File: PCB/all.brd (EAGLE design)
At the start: 49.8 x 49.8 mm, 41 parts, among them J1 ISP Programmer, U1 ATMEGA32U4, U2 3.3V_REG, U3 MPU-6050-1, U5 MCP73831, U6 AL8805, X1 USBSMD

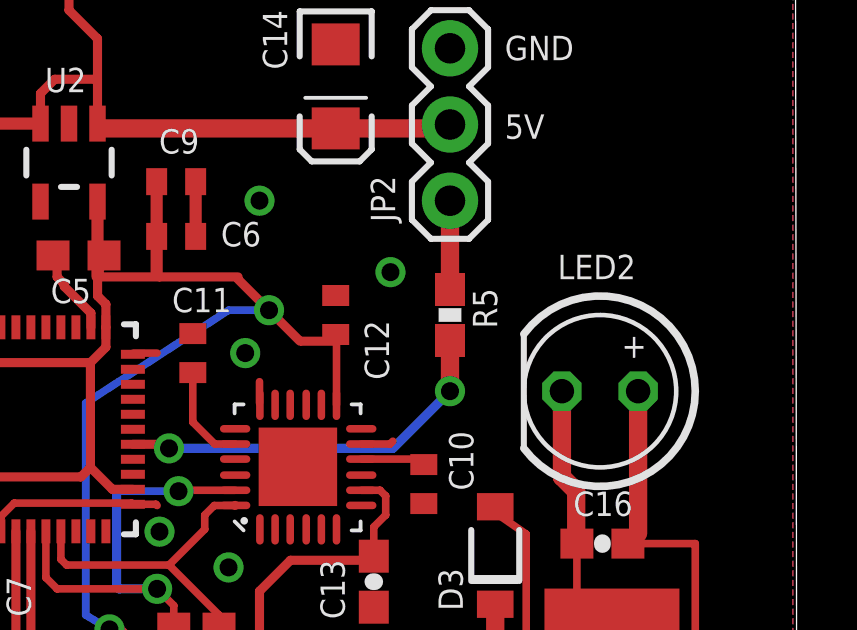
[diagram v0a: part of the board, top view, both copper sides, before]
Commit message: added 3D models
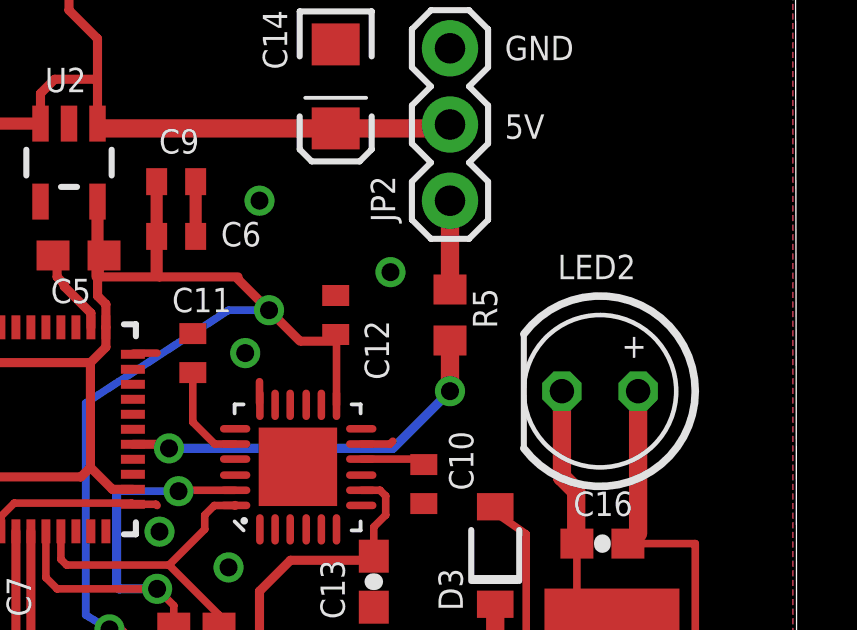
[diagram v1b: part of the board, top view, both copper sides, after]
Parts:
- R5: device SparkFun:0603-RES -> rcl:R0603
- U1: device SparkFun:QFN-44-NOPAD -> SparkFun-Retired:SPARKFUN-DIGITALIC_QFN-44-NOPAD
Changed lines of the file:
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@@
 <?xml version="1.0" encoding="utf-8"?>
 <!DOCTYPE eagle SYSTEM "eagle.dtd">
-<eagle version="7.4.0">
+<eagle version="7.3.0">
 <drawing>
 <settings>
@@
 <layers>
 <layer number="1" name="Top" color="4" fill="1" visible="yes" active="yes"/>
+<layer number="2" name="Route2" color="1" fill="3" visible="no" active="yes"/>
+<layer number="3" name="Route3" color="4" fill="3" visible="no" active="yes"/>
+<layer number="4" name="Route4" color="1" fill="4" visible="no" active="yes"/>
+<layer number="5" name="Route5" color="4" fill="4" visible="no" active="yes"/>
+<layer number="6" name="Route6" color="1" fill="8" visible="no" active="yes"/>
+<layer number="7" name="Route7" color="4" fill="8" visible="no" active="yes"/>
+<layer number="8" name="Route8" color="1" fill="2" visible="no" active="yes"/>
+<layer number="9" name="Route9" color="4" fill="2" visible="no" active="yes"/>
+<layer number="10" name="Route10" color="1" fill="7" visible="no" active="yes"/>
+<layer number="11" name="Route11" color="4" fill="7" visible="no" active="yes"/>
+<layer number="12" name="Route12" color="1" fill="5" visible="no" active="yes"/>
+<layer number="13" name="Route13" color="4" fill="5" visible="no" active="yes"/>
+<layer number="14" name="Route14" color="1" fill="6" visible="no" active="yes"/>
+<layer number="15" name="Route15" color="4" fill="6" visible="no" active="yes"/>
 <layer number="16" name="Bottom" color="1" fill="1" visible="yes" active="yes"/>
 <layer number="17" name="Pads" color="2" fill="1" visible="yes" active="yes"/>
@@
 <layer number="54" name="bGND_GNDA" color="1" fill="9" visible="no" active="no"/>
 <layer number="56" name="wert" color="7" fill="1" visible="no" active="no"/>
+<layer number="57" name="tCAD" color="7" fill="1" visible="no" active="no"/>
+<layer number="59" name="tCarbon" color="7" fill="1" visible="no" active="no"/>
+<layer number="60" name="bCarbon" color="7" fill="1" visible="no" active="no"/>
+<layer number="90" name="Modules" color="5" fill="1" visible="no" active="no"/>
 <layer number="91" name="Nets" color="2" fill="1" visible="no" active="no"/>
 <layer number="92" name="Busses" color="1" fill="1" visible="no" active="no"/>
@@
 <layer number="108" name="tplace-old" color="10" fill="1" visible="no" active="yes"/>
 <layer number="109" name="ref-old" color="11" fill="1" visible="no" active="yes"/>
+<layer number="110" name="fp0" color="7" fill="1" visible="no" active="yes"/>
+<layer number="111" name="LPC17xx" color="7" fill="1" visible="no" active="yes"/>
+<layer number="112" name="tSilk" color="7" fill="1" visible="no" active="yes"/>
+<layer number="113" name="IDFDebug" color="4" fill="1" visible="no" active="yes"/>
 <layer number="116" name="Patch_BOT" color="9" fill="4" visible="no" active="yes"/>
 <layer number="121" name="_tsilk" color="7" fill="1" visible="no" active="yes"/>
 <layer number="122" name="_bsilk" color="7" fill="1" visible="no" active="yes"/>
+<layer number="123" name="tTestmark" color="7" fill="1" visible="no" active="yes"/>
+<layer number="124" name="bTestmark" color="7" fill="1" visible="no" active="yes"/>
 <layer number="125" name="_tNames" color="7" fill="1" visible="no" active="yes"/>
+<layer number="126" name="_bNames" color="7" fill="1" visible="no" active="yes"/>
+<layer number="127" name="_tValues" color="7" fill="1" visible="no" active="yes"/>
+<layer number="128" name="_bValues" color="7" fill="1" visible="no" active="yes"/>
+<layer number="129" name="Mask" color="7" fill="1" visible="yes" active="yes"/>
+<layer number="131" name="tAdjust" color="7" fill="1" visible="no" active="yes"/>
+<layer number="132" name="bAdjust" color="7" fill="1" visible="no" active="yes"/>
 <layer number="144" name="Drill_legend" color="7" fill="1" visible="no" active="yes"/>
+<layer number="150" name="Notes" color="7" fill="1" visible="no" active="yes"/>
 <layer number="151" name="HeatSink" color="7" fill="1" visible="no" active="yes"/>
+<layer number="152" name="_bDocu" color="7" fill="1" visible="no" active="yes"/>
+<layer number="153" name="FabDoc1" color="7" fill="1" visible="no" active="yes"/>
+<layer number="154" name="FabDoc2" color="7" fill="1" visible="no" active="yes"/>
+<layer number="155" name="FabDoc3" color="7" fill="1" visible="no" active="yes"/>
 <layer number="199" name="Contour" color="7" fill="1" visible="no" active="yes"/>
 <layer number="200" name="200bmp" color="1" fill="10" visible="no" active="yes"/>
@@
 <layer number="220" name="220bmp" color="21" fill="1" visible="no" active="no"/>
 <layer number="221" name="221bmp" color="22" fill="1" visible="no" active="no"/>
-<layer number="222" name="222bmp" color="23" fill="1" visible="no" active="no"/>
 <layer number="223" name="223bmp" color="24" fill="1" visible="no" active="no"/>
 <layer number="224" name="224bmp" color="25" fill="1" visible="no" active="no"/>
+<layer number="225" name="225bmp" color="7" fill="1" visible="yes" active="yes"/>
+<layer number="226" name="226bmp" color="7" fill="1" visible="yes" active="yes"/>
+<layer number="227" name="227bmp" color="7" fill="1" visible="yes" active="yes"/>
+<layer number="228" name="228bmp" color="7" fill="1" visible="yes" active="yes"/>
+<layer number="229" name="229bmp" color="7" fill="1" visible="yes" active="yes"/>
+<layer number="230" name="230bmp" color="7" fill="1" visible="yes" active="yes"/>
+<layer number="231" name="231bmp" color="7" fill="1" visible="yes" active="yes"/>
+<layer number="248" name="Housing" color="7" fill="1" visible="no" active="yes"/>
+<layer number="249" name="Edge" color="7" fill="1" visible="no" active="yes"/>
 <layer number="250" name="Descript" color="3" fill="1" visible="no" active="no"/>
 <layer number="251" name="SMDround" color="12" fill="11" visible="no" active="no"/>
 <layer number="254" name="cooling" color="7" fill="1" visible="no" active="yes"/>
+<layer number="255" name="routoute" color="7" fill="1" visible="yes" active="yes"/>
 </layers>
 <board>
@@
 </autorouter>
 <elements>
-<element name="U1" library="SparkFun" package="QFN-44-NOPAD" value="ATMEGA32U4" x="24.13" y="21.59" smashed="yes">
+<element name="U1" library="SparkFun-Retired" package="SPARKFUN-DIGITALIC_QFN-44-NOPAD" value="ATMEGA32U4" x="24.13" y="21.59" smashed="yes">
 <attribute name="NAME" x="19.29875" y="24.881875" size="0.8128" layer="25"/>
 <attribute name="VALUE" x="21.63" y="15.44" size="1.27" layer="27"/>
@@
 <attribute name="VALUE" x="41.275" y="27.94" size="1.27" layer="27" rot="R90"/>
 </element>
-<element name="R5" library="SparkFun" package="0603-RES" value="300" x="38.1" y="25.4" smashed="yes" rot="R270">
+<element name="R5" library="rcl" package="R0603" value="300" x="38.1" y="25.4" smashed="yes" rot="R270">
 <attribute name="NAME" x="38.862" y="26.289" size="0.8128" layer="25" font="vector" rot="R270"/>
 <attribute name="VALUE" x="36.957" y="26.416" size="0.4064" layer="27" font="vector" rot="R270"/>

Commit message: Adding Qi receiver modules
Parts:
- removed F1: PTCSMD, SparkFun:PTC-1206
- removed XTAL1: 16MHz, SparkFun:CRYSTAL-SMD-5X3
- added C18, C19, C20, C21, C22, C23, C24, C25, C26, C27, C28, C29: 10μF, SparkFun:EIA3216
- added CP1, CP2, CP3, CP4, CP5, CP6, CP7, CP8, CS, CS10, CS17, CS20, CS27, CS30, CS37, CS7: 18pF, rcl:C0603
- added CS1, CS11, CS12, CS2, CS21, CS22, CS31, CS32: 10nF, rcl:C0603
- added CS13, CS15, CS23, CS25, CS3, CS33, CS35, CS5: 0.47μF, rcl:C0603
- added CS14, CS16, CS24, CS26, CS34, CS36, CS4, CS6: 22nF, rcl:C0603
- added CS18, CS19, CS28, CS29, CS38, CS39, CS8, CS9: 100nF, rcl:C0603
- added J3, J4, J5, J6: (no value), SparkFun-Connectors:1X02_BIG
- added R10, R11, R14, R17: 10k, rcl:R0603
- added R12, R15, R4: 188, rcl:R0603
- added R13, R16, R9: 230, rcl:R0603
- added U$1: Loveread Lamp v2.0, frames:A4L-LOC
- added U4, U7, U8, U9: BQ51013B_RHL_20, pero_library:RHL20_2P05X3P05
- L1: value 33 μH -> 56uH
- R2: value 22 -> 188
- R3: value 22 -> 230
- X1: value USBSMD -> 8MHz; device SparkFun:USB-MINIB -> pero_library:6X3.2MM
- moved R2 261.0 mm to (-107.5, -207.5)
- moved R3 251.6 mm to (-112.5, -192.5)
- moved X1 227.9 mm to (-112.5, -170.0)
- moved C13 2.85 mm to (33.0, 15.3)
- moved JP2 2.85 mm to (35.5, 28.0)
- moved L1 2.85 mm to (40.9, 12.6)
- moved D3 2.85 mm to (37.0, 16.2)
- moved LED2 2.85 mm to (40.5, 21.7)
- moved R5 2.85 mm to (35.5, 24.2)
- moved RS 2.85 mm to (34.9, 12.6)
- moved U3 2.85 mm to (30.4, 19.1)
- moved D1 2.85 mm to (17.7, 34.4)
- moved J2 2.85 mm to (3.28, 34.4)
- moved C1 2.85 mm to (19.4, 25.6)
- moved C14 2.85 mm to (31.7, 31.8)
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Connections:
- removed net D+: R2.1, X1.D+
- removed net D-: R3.1, X1.D-
- new net N$10: CS.1, CS7.1, J3.P$2
- new net N$11: CP1.1, CP2.1, CS2.1, CS3.1, CS4.1, J3.P$1, U4.19
- new net N$12: CS1.2, U4.3
- new net N$13: CS2.2, U4.17
- new net N$14: CS3.2, U4.16
- new net N$19: CS4.2, U4.15
- new net N$20: CS6.2, U4.6
- new net N$21: CS5.2, U4.5
- new net N$22: CS12.2, U7.17
- new net N$23: C20.A, C21.A, CS9.1, U4.18
- new net N$24: R9.2, U4.12
- new net N$25: R4.2, R9.1, U4.14
- new net N$26: R10.1, U4.13
- new net N$27: CS13.2, U7.16
- new net N$28: CS14.2, U7.15
- new net N$29: CS16.2, U7.6
- new net N$30: CS15.2, U7.5
- new net N$31: CP3.2, CP4.2, CS10.2, CS11.1, CS15.1, CS16.1, CS17.2, U7.2
- new net N$32: C22.A, C23.A, CS19.1, U7.18
- new net N$33: R3.2, U7.12
- new net N$34: R2.2, R3.1, U7.14
- new net N$35: R11.1, U7.13
- new net N$36: CS20.1, CS27.1, J5.P$2
- new net N$37: CP5.1, CP6.1, CS22.1, CS23.1, CS24.1, J5.P$1, U8.19
- new net N$38: CS21.2, U8.3
- new net N$39: CS22.2, U8.17
- new net N$40: CS23.2, U8.16
- new net N$41: CS24.2, U8.15
- new net N$42: CS26.2, U8.6
- new net N$43: CS25.2, U8.5
- new net N$44: CP5.2, CP6.2, CS20.2, CS21.1, CS25.1, CS26.1, CS27.2, U8.2
- new net N$45: C25.A, C26.A, CS29.1, U8.18
- new net N$46: R13.2, U8.12
- new net N$47: R12.2, R13.1, U8.14
- new net N$48: R14.1, U8.13
- new net N$49: CS30.1, CS37.1, J6.P$2
- new net N$50: CP7.1, CP8.1, CS32.1, CS33.1, CS34.1, J6.P$1, U9.19
- new net N$51: CS31.2, U9.3
- new net N$52: CS32.2, U9.17
- new net N$53: CS33.2, U9.16
- new net N$54: CS34.2, U9.15
- new net N$55: CS36.2, U9.6
- new net N$56: CS35.2, U9.5
- new net N$57: CP7.2, CP8.2, CS30.2, CS31.1, CS35.1, CS36.1, CS37.2, U9.2
- new net N$58: C28.A, C29.A, CS39.1, U9.18
- new net N$59: R16.2, U9.12
- new net N$60: R15.2, R16.1, U9.14
- new net N$61: R17.1, U9.13
- new net N$9: CP1.2, CP2.2, CS.2, CS1.1, CS5.1, CS6.1, CS7.2, U4.2
- new net V_QI1: C18.A, CS18.1, U7.4
- new net V_QI2: C19.A, CS8.1, U4.4
- new net V_QI3: C24.A, CS28.1, U8.4
- new net V_QI4: C27.A, CS38.1, U9.4
- net GND: now also C18.C, C19.C, C20.C, C21.C, C22.C, C23.C, C24.C, C25.C, C26.C, C27.C, C28.C, C29.C, CS18.2, CS19.2, CS28.2, CS29.2, CS38.2, CS39.2, CS8.2, CS9.2, R10.2, R11.2, R12.1, R14.2, R15.1, R17.2, R2.1, R4.1, U4.1, U4.10, U4.11, U4.20, U4.21, U4.9, U7.1, U7.10, U7.11, U7.20, U7.21, U7.9, U8.1, U8.10, U8.11, U8.20, U8.21, U8.9, U9.1, U9.10, U9.11, U9.20, U9.21, U9.9; no longer X1.GND
- net N$16: now also CS11.2, U7.3; no longer F1.1, X1.VBUS
- net N$2: now also X1.P$2; no longer XTAL1.3
- net N$3: now also X1.P$1; no longer XTAL1.1
- net N$4: no longer F1.2, U1.2, U1.7
- net N$6: now also CS10.1, CS17.1, J4.P$2; no longer R2.2, U1.4
- net N$8: now also CP3.1, CP4.1, CS12.1, CS13.1, CS14.1, J4.P$1, U7.19; no longer R3.2, U1.3
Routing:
- net 5V: track 124.2 -> 138.1 mm
- net N$4: track 19.8 -> 6.62 mm
- net PD7: track 13.1 -> 19.0 mm
- net 3.3V: track 74.4 -> 80.0 mm
- net N$8: track 5.14 -> 0.00 mm
- net N$6: track 4.75 -> 0.00 mm
- net N$16: track 4.29 -> 0.00 mm
- net SCL: track 15.5 -> 18.8 mm
- net D-: track 3.22 -> 0.00 mm
- net D+: track 3.00 -> 0.00 mm
- net N$3: track 9.50 -> 7.31 mm
- net N$2: track 12.9 -> 11.3 mm
- net PB7: track 25.0 -> 23.8 mm
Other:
- board size 49.8 x 49.8 mm -> 45 x 45 mm
- board text added: "July, 2016"
- board text added: "Loveread Lamp"
- board text added: "Loveread Lamp v2.0 Pero 2016"
- board text added: "Pero"
- board text added: "Prelimirary board layout 26.7.2016"
- board text added: "v2.0"
- board text removed: "GND CONNECTION MISSING!!!"
- board text removed: "Loveread Lamp Pero 2015"
- board text removed: "THERE IS A PAD-PLANE CONTACT HERE!!"

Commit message: Adding Tiny163 4 instead of mega32u4
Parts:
- removed C1, C4: 0.1μF, rcl:C0402
- removed C2, C3: 18pF, rcl:C0603
- removed X1: 8MHz, pero_library:6X3.2MM
- added J7: (no value), SparkFun-Connectors:1X02
- U1: value ATMEGA32U4 -> ATTINY1634MLF20; device SparkFun-Retired:SPARKFUN-DIGITALIC_QFN-44-NOPAD -> attiny1634:MLF20
- moved U1 339.9 mm to (-122.5, -287.5)
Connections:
- removed net AREF: C1.1, U1.42
- removed net MOSI: J1.4, U1.10
- removed net N$2: C2.2, U1.17, X1.P$2
- removed net N$3: C3.2, U1.16, X1.P$1
- removed net PB0: U1.8
- removed net PB4: U1.28
- removed net PB5: U1.29
- removed net PB6: U1.30
- removed net PC6: U1.31
- removed net PC7: U1.32
- removed net PD4: U1.25
- removed net PD5: U1.22
- removed net PD6: U1.26
- removed net PE6: U1.1
- removed net PF0: U1.41
- removed net PF1: U1.40
- removed net PF4: U1.39
- removed net PF5: U1.38
- removed net PF6: U1.37
- removed net PF7: U1.36
- removed net SCK: J1.3, U1.9
- removed net UCAP: C4.1, U1.6
- net 3.3V: now also U1.9, U3.9; no longer U1.14, U1.24, U1.34, U1.44
- net GND: now also U1.8, U1.GND; no longer C1.2, C2.1, C3.1, C4.2, U1.15, U1.23, U1.33, U1.35, U1.43, U1.5
- net MISO: now also U1.17; no longer U1.11
- net PB7: no longer U1.12
- net PD7: no longer U1.27
- net RST: now also U1.12; no longer U1.13
- net RX: now also J7.1
- net SCL: now also J1.3, U1.14; no longer U1.18
- net SDA: now also J1.4, U1.18; no longer U1.19
- net TX: now also J7.2, U1.19; no longer U1.21
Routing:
- net 3.3V: track 80.0 -> 61.5 mm
- net MOSI: track 17.6 -> 0.00 mm
- net GND: track 25.0 -> 7.84 mm
- net SDA: track 10.7 -> 27.4 mm
- net SCK: track 16.4 -> 0.00 mm
- net SCL: track 18.8 -> 33.6 mm
- net N$2: track 11.3 -> 0.00 mm
- net N$3: track 7.31 -> 0.00 mm
- net UCAP: track 5.07 -> 0.00 mm
- net RST: track 26.0 -> 23.1 mm
- net MISO: track 12.7 -> 10.5 mm
- net PB7: track 23.8 -> 21.7 mm
- net AREF: track 1.76 -> 0.00 mm
- net PD7: track 19.0 -> 18.0 mm

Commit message: Two-sheet schematics, and routing Qi chargers
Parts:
- removed LED2: High Power White LED, led:LED5MM
- added D4, D5, D6: SMF5.0AT1, diode:SOD123FL
- added J8: BL-HP20AUW2C, SparkFun-Connectors:1X02
- moved U1 340.0 mm to (22.5, 20.0)
- moved R12 277.3 mm to (42.4, -17.5), turned to 90 degrees
- moved R14 275.6 mm to (44.4, -17.5), turned to 270 degrees
- moved C26 271.7 mm to (42.7, -29.4), turned to 90 degrees
- moved C24 267.6 mm to (47.5, -24.2), turned to 90 degrees
- moved J5 265.3 mm to (29.8, -25.4), turned to 270 degrees
- moved R13 263.8 mm to (40.4, -17.5), turned to 270 degrees
- moved CS22 262.6 mm to (36.0, -20.9), turned to 90 degrees
- moved J6 259.2 mm to (-2.70, -55.4), turned to 270 degrees
- moved CS27 256.9 mm to (32.5, -30.4)
- moved CS24 256.3 mm to (32.1, -20.9), turned to 90 degrees
- moved CP5 256.1 mm to (32.5, -26.5)
- moved C25 255.2 mm to (40.1, -29.4), turned to 90 degrees
- moved CP6 253.8 mm to (32.5, -24.5)
- moved CS28 253.2 mm to (45.2, -23.7), turned to 270 degrees
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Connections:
- removed net N$4: C15.A, D2.A, U5.4
- removed net PB7: U6.3
- removed net PD7: R5.2
- new net PWM: U1.15, U6.3
- new net RGB: R5.2, U1.1
- new net V_QI_IN: C15.A, D2.C, D4.C, D5.C, D6.C, U5.4
- net 5V: no longer D2.C
- net ANODE: no longer LED2.A
- net CATHODE: no longer LED2.K
- net V_QI1: now also D2.A
- net V_QI2: now also D4.A
- net V_QI3: now also D5.A
- net V_QI4: now also D6.A
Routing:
- net 5V: track 138.1 -> 25.9 mm, vias 4 -> 0
- net 3.3V: track 61.5 -> 27.6 mm, vias 2 -> 0
- net SCL: track 33.6 -> 0.00 mm, vias 2 -> 0
- net SDA: track 27.4 -> 0.00 mm
- net RST: track 23.1 -> 0.00 mm
- net N$42: track 0.00 -> 22.8 mm, vias 0 -> 2
- net N$78: track 0.00 -> 22.8 mm, vias 0 -> 2
- net N$65: track 0.00 -> 22.7 mm, vias 0 -> 2
- net N$29: track 0.00 -> 22.7 mm, vias 0 -> 2
- net N$37: track 0.00 -> 21.8 mm
- net N$11: track 0.00 -> 21.8 mm
- net PWM: track 0.00 -> 21.7 mm, vias 0 -> 2
- net PB7: track 21.7 -> 0.00 mm, vias 2 -> 0
- net N$67: track 0.00 -> 19.6 mm
- net N$31: track 0.00 -> 19.6 mm
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- added copper zone on layer 1, net N$31
- added copper zone on layer 1, net N$44
- added copper zone on layer 1, net N$67
- added copper zone on layer 1, net N$80

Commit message: Qi chargers routed
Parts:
- moved D6 370.3 mm to (1.60, 31.4), turned to 90 degrees
- moved J8 356.6 mm to (-7.50, 12.5), turned to 90 degrees
- moved C29 354.9 mm to (6.05, 42.0), turned to 270 degrees
- moved CS37 350.3 mm to (16.5, 43.2), turned to 180 degrees
- moved D5 347.0 mm to (25.4, 3.90), turned to 90 degrees
- moved J7 344.7 mm to (-7.50, 27.5), turned to 90 degrees
- moved C28 344.7 mm to (8.80, 42.0), turned to 270 degrees
- moved CP7 344.0 mm to (16.6, 39.3), turned to 180 degrees
- moved C27 339.8 mm to (1.75, 36.8), turned to 270 degrees
- moved CP8 339.5 mm to (16.5, 37.2), turned to 180 degrees
- moved R15 339.3 mm to (6.60, 30.2), turned to 270 degrees
- moved R17 337.0 mm to (4.70, 30.3), turned to 90 degrees
- moved CS30 336.4 mm to (16.5, 41.1), turned to 180 degrees
- moved CS32 335.6 mm to (13.0, 33.8), turned to 270 degrees
- moved CS34 334.4 mm to (17.0, 33.8), turned to 270 degrees
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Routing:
- net N$55: track 0.00 -> 199.1 mm, vias 0 -> 2
- net N$56: track 0.00 -> 198.1 mm, vias 0 -> 2
- net N$58: track 0.00 -> 195.0 mm, vias 0 -> 2
- net N$20: track 0.00 -> 192.0 mm, vias 0 -> 2
- net N$21: track 0.00 -> 188.8 mm, vias 0 -> 2
- net N$23: track 0.00 -> 187.9 mm, vias 0 -> 2
- net N$30: track 15.5 -> 90.3 mm
- net N$29: track 22.7 -> 95.2 mm
- net N$43: track 15.5 -> 85.6 mm
- net N$32: track 11.7 -> 81.3 mm
- net N$45: track 11.7 -> 79.6 mm
- net N$42: track 22.8 -> 88.1 mm
- net N$78: track 22.8 -> 0.00 mm, vias 2 -> 0
- net N$65: track 22.7 -> 0.00 mm, vias 2 -> 0
- net N$57: track 0.00 -> 19.6 mm
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- added copper zone on layer 1, net N$57
- added copper zone on layer 1, net N$9
- removed copper zone on layer 1, net N$67
- removed copper zone on layer 1, net N$80

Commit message: LED driver changed
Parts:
- removed C16: 2.2μF, SparkFun:0603-CAP
- removed D1: SMF5.0AT1, diode:SOD123FL
- removed RS: 10k, rcl:R0603
- added C1: 10μF, rcl:C0603
- added Q1, Q2: (no value), SparkFun-DiscreteSemi:SOT23-3
- added R18: (no value), rcl:R0603
- added R19: 1, resistor:R0603
- added R20: 1k, resistor:R0603
- added SJ1, SJ2: (no value), SparkFun-Retired:SJ_3_PASTE2&3
- L1: value 56uH -> 22uH
- U6: value AL8805 -> CAT4139; device pero_library2:SOT23-5 -> pero_library:SOT23-5
- moved U6 244.0 mm to (-125.0, -66.2), turned to 0 degrees
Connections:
- removed net ANODE: C16.2, U6.4
- removed net CATHODE: C16.1, L1.P$2
- new net N$2: Q1.2, Q2.1, R18.2
- new net N$3: Q1.1, Q2.3, SJ1.3
- new net N$4: SJ1.1, U6.4
- new net N$62: J8.1, SJ2.2
- new net N$63: D3.A, L1.P$2, U6.1
- new net N$64: C17.1, D3.C, SJ2.1
- new net N$65: R20.1, U6.3
- net 5V: now also C1.1, L1.P$1, SJ2.3; no longer C17.1, D1.C, D3.C, RS.1
- net GND: now also C1.2, Q2.2, R18.1, R19.2
- net N$18: now also J8.2, Q1.3, R19.1, R20.2; no longer D3.A, L1.P$1, RS.2, U6.1
- net PWM: now also SJ1.2; no longer U6.3
- net VBAT: no longer D1.A
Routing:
- net N$18: track 18.6 -> 0.00 mm
- net ANODE: track 17.9 -> 0.00 mm
- net 5V: track 25.9 -> 14.5 mm
- net PWM: track 5.93 -> 0.00 mm
- net CATHODE: track 3.06 -> 0.00 mm
